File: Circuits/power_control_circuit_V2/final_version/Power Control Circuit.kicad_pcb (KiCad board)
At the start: 2 copper layers, 122.3 x 43.4 mm, 38 parts, among them Q10 IRF1405, Q12 IRF1405, Q2 S8050, Q3 S8550, Q4 IRF1405, Q6 S8050, Q7 S8550, Q8 IRF1405, Q9 IRF1405, U1 PC817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

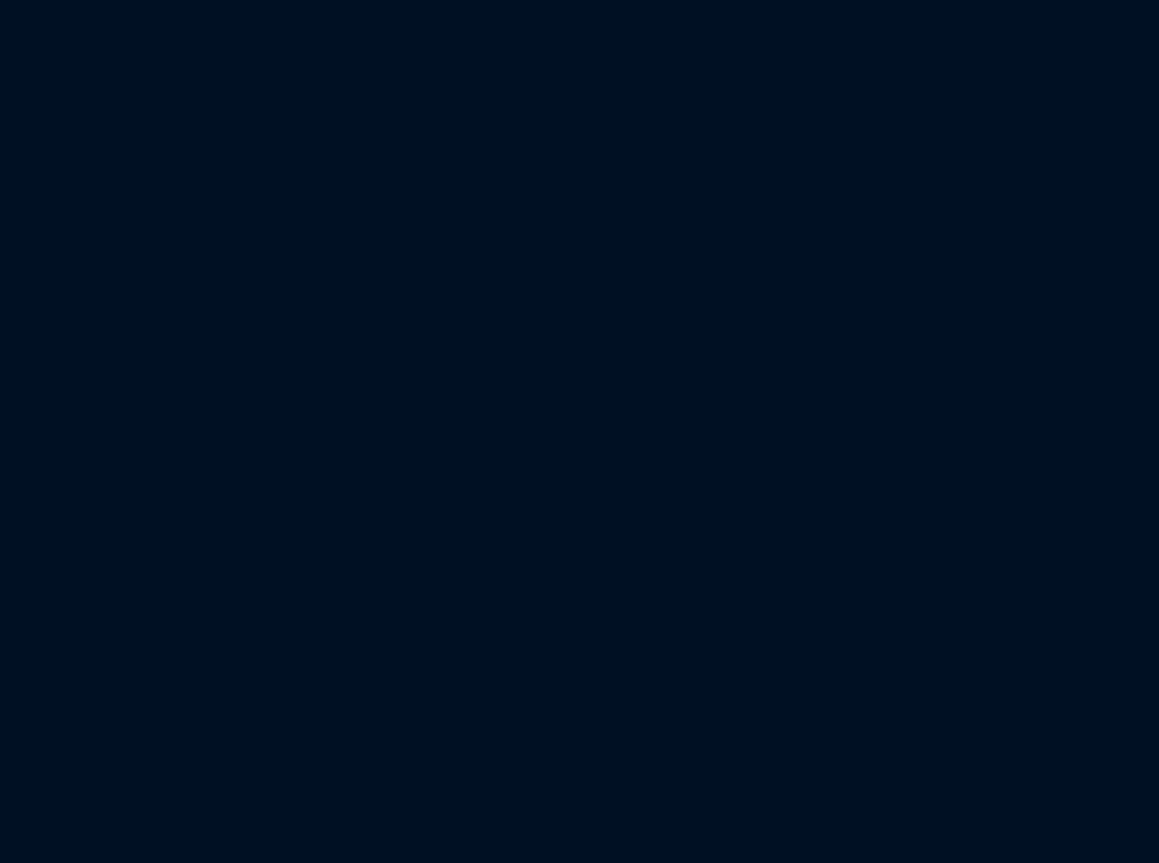
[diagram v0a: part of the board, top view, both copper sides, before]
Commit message: started pad changes
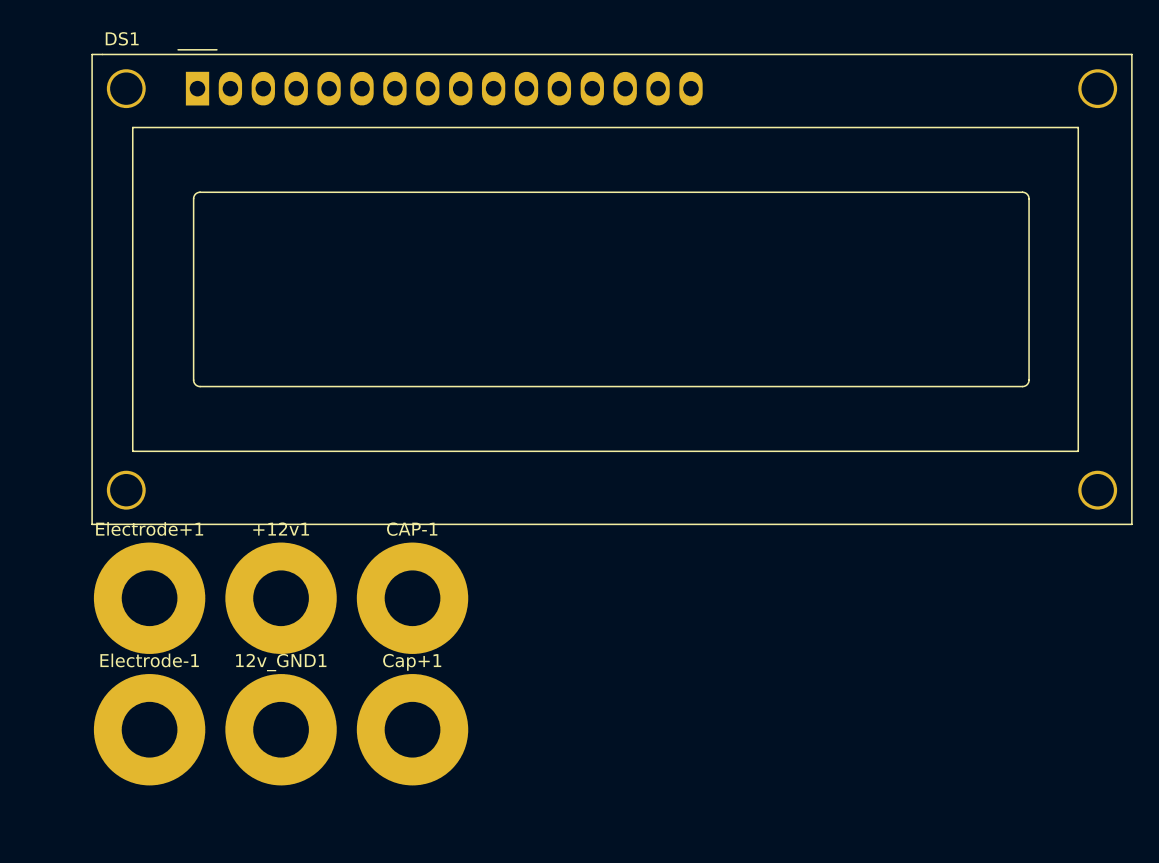
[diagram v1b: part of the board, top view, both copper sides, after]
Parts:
- added +12v1: Pin, MountingHole:MountingHole_4.3mm_M4_Pad, F.Cu at (108.0, 91.2)
- added 12v_GND1: Pin, MountingHole:MountingHole_4.3mm_M4_Pad, F.Cu at (108.0, 101.3)
- added CAP-1: Pin, MountingHole:MountingHole_4.3mm_M4_Pad, F.Cu at (118.2, 91.2)
- added Cap+1: Pin, MountingHole:MountingHole_4.3mm_M4_Pad, F.Cu at (118.2, 101.3)
- added DS1: WC1602A, Display:WC1602A, F.Cu at (101.6, 51.8)
- added Electrode+1: Pin, MountingHole:MountingHole_4.3mm_M4_Pad, F.Cu at (97.9, 91.2)
- added Electrode-1: Pin, MountingHole:MountingHole_4.3mm_M4_Pad, F.Cu at (97.9, 101.3)
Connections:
- net Net-(Q4-D) renamed /NMOS_CHARGE
- Q10 pad 1: Net-(Electrodes1-Pin_1) -> /NMOS_DISCHARGE
- Q12 pad 1: Net-(Electrodes1-Pin_1) -> /NMOS_DISCHARGE
- Q8 pad 1: Net-(Electrodes1-Pin_1) -> /NMOS_DISCHARGE
- Q9 pad 1: Net-(Electrodes1-Pin_1) -> /NMOS_DISCHARGE

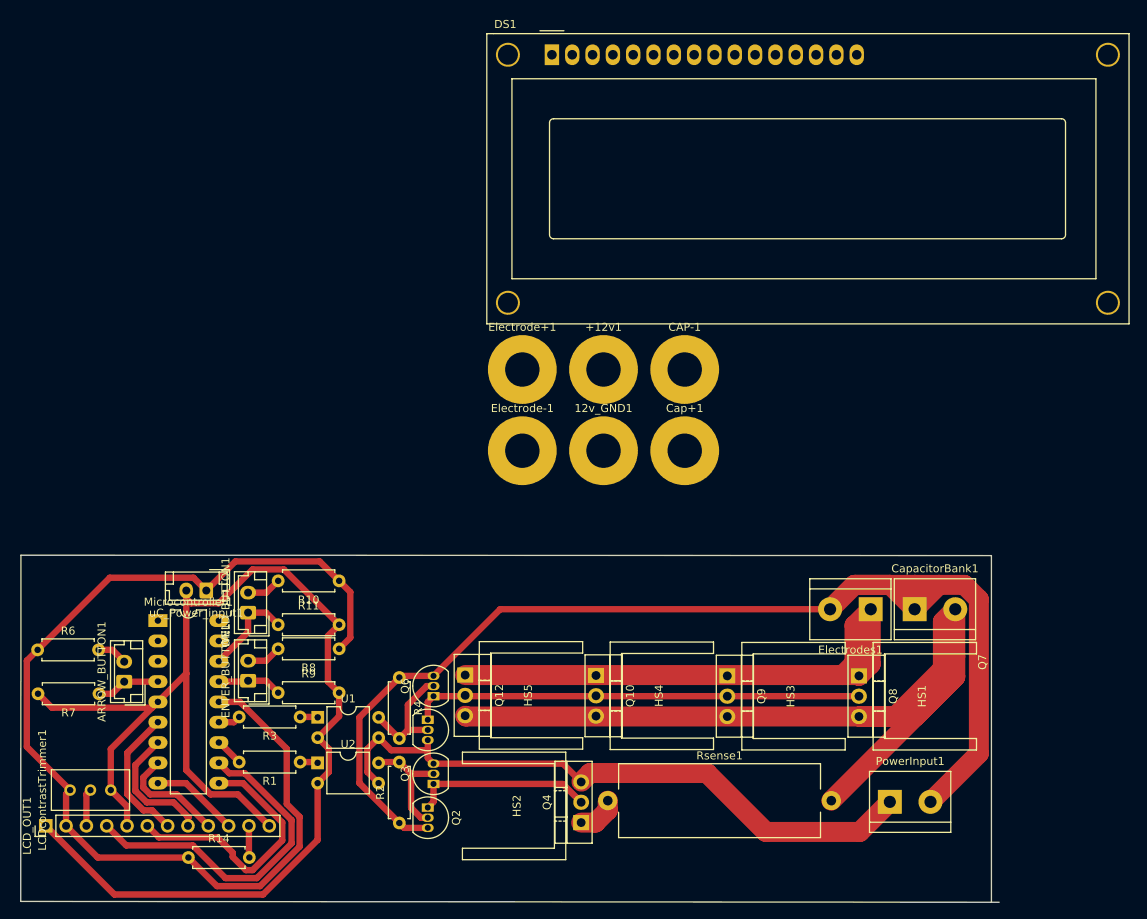
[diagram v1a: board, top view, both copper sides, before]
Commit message: added terminal pads to the pcb
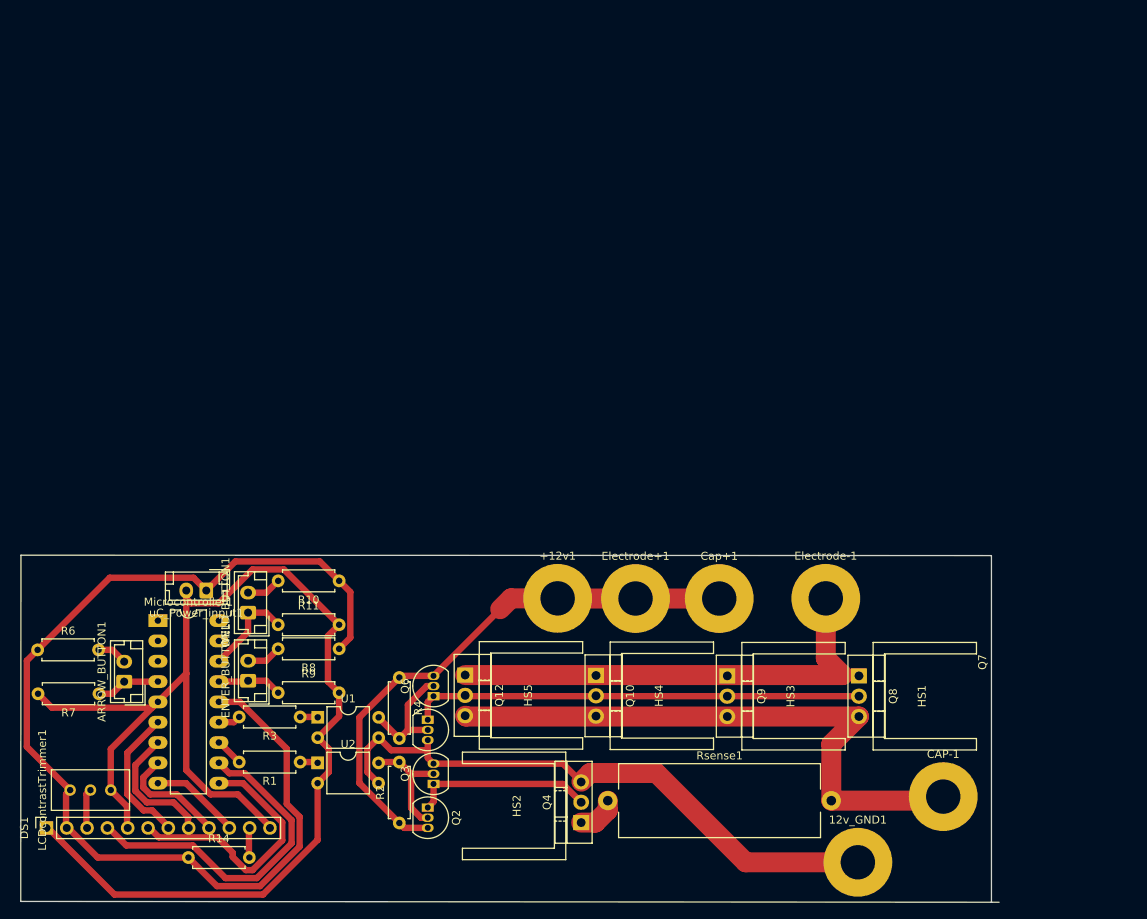
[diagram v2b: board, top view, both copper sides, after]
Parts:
- removed CapacitorBank1: CP, TerminalBlock:TerminalBlock_bornier-2_P5.08mm
- removed Electrodes1: Conn_01x02_Male, TerminalBlock:TerminalBlock_bornier-2_P5.08mm
- removed LCD_OUT1: Conn_01x12_Socket, Connector_PinHeader_2.54mm:PinHeader_1x12_P2.54mm_Vertical
- removed PowerInput1: Screw_Terminal_01x02, TerminalBlock:TerminalBlock_bornier-2_P5.08mm
- DS1: footprint Display:WC1602A -> Connector_PinSocket_2.54mm:PinSocket_1x12_P2.54mm_Vertical
- moved DS1 115.5 mm to (38.4, 148.5), turned to 90 degrees
- moved CAP-1 62.4 mm to (150.5, 144.6)
- moved 12v_GND1 60.5 mm to (139.8, 152.8)
- moved Electrode-1 42.2 mm to (135.8, 119.8)
- moved Electrode+1 31.9 mm to (112.0, 119.8)
- moved +12v1 29.2 mm to (102.3, 119.8)
- moved Cap+1 19.0 mm to (122.5, 119.8)
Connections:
- DS1 pad 10: unconnected-(DS1-D3-Pad10) -> D7
- DS1 pad 11: D4 -> LED+
- DS1 pad 12: D5 -> GND
- DS1 pad 7: unconnected-(DS1-D0-Pad7) -> D4
- DS1 pad 8: unconnected-(DS1-D1-Pad8) -> D5
- DS1 pad 9: unconnected-(DS1-D2-Pad9) -> D6
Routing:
- net +12V: track 148.1 -> 70.2 mm
- net Net-(Electrodes1-Pin_1): track 67.9 -> 0.00 mm
- net /NMOS_DISCHARGE: track 0.00 -> 57.7 mm
- net GNDS: track 117.0 -> 75.4 mm
- net GNDA: track 79.9 -> 75.9 mm

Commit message: redesigning the circuit
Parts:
- removed ARROW_BUTTON1, ENTER_BUTTON1, WELD_BUTTON1, uC_Power_input1: Conn_01x02_Socket, Connector_JST:JST_EH_B2B-EH-A_1x02_P2.50mm_Vertical
- removed HS1, HS2, HS3, HS4, HS5: Heatsink_Pad_2Pin, Heatsink:Heatsink_Stonecold_HS-S03_13.21x12.7mm
- removed LCDcontrastTrimmer1: 5kOhm, Potentiometer_THT:Potentiometer_Bourns_3386C_Horizontal
- removed Microcontroller1: PIC16F628A-IP, Package_DIP:DIP-18_W7.62mm_LongPads
- added ARROW1: JST-2P, Connector_JST:JST_EH_B2B-EH-A_1x02_P2.50mm_Vertical, F.Cu at (58.4, 104.1)
- added ENTER1: JST-2P, Connector_JST:JST_EH_B2B-EH-A_1x02_P2.50mm_Vertical, F.Cu at (80.0, 105.4)
- added Main-MCU1: PIC16F628A-IP, Package_DIP:DIP-18_W7.62mm_LongPads, F.Cu at (64.8, 96.5)
- added Power5v1: JST-2P, Connector_JST:JST_EH_B2B-EH-A_1x02_P2.50mm_Vertical, F.Cu at (55.4, 91.9)
- added Trimmer1: 5kOhm, Connector_PinSocket_2.54mm:PinSocket_1x03_P2.54mm_Vertical, F.Cu at (46.7, 124.2)
- added WELD1: JST-2P, Connector_JST:JST_EH_B2B-EH-A_1x02_P2.50mm_Vertical, F.Cu at (80.0, 96.5)
- moved Q12 73.2 mm to (160.5, 107.2), turned to 0 degrees
- moved Q10 46.9 mm to (148.3, 107.2), turned to 0 degrees
- moved Electrode+1 45.3 mm to (148.8, 93.5)
- moved +12v1 43.3 mm to (136.7, 93.5)
- moved R2 40.7 mm to (104.6, 113.8)
- moved Electrode-1 38.7 mm to (165.1, 94.5)
- moved Q2 36.1 mm to (111.3, 120.0), turned to 90 degrees
- moved Q6 34.2 mm to (111.3, 108.2)
- moved Q7 34.1 mm to (110.7, 111.5)
- moved Q4 32.6 mm to (128.0, 124.5), turned to 180 degrees
- moved Rsense1 32.1 mm to (134.4, 126.0)
- moved R11 31.8 mm to (85.6, 97.0)
- moved U1 31.6 mm to (93.5, 111.2)
- moved U2 30.9 mm to (93.5, 117.9)
- moved Q3 30.8 mm to (110.7, 123.7), turned to -90 degrees
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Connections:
- net LED+ renamed Net-(DS1-LED(+))
- DS1 pad 3: VO -> Net-(DS1-VO)
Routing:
- net GND: track 170.1 -> 0.00 mm
- net +5V: track 137.4 -> 0.00 mm
- net GNDA: track 75.9 -> 0.00 mm
- net GNDS: track 75.4 -> 0.00 mm
- net +12V: track 70.2 -> 0.00 mm
- net /NMOS_DISCHARGE: track 57.7 -> 0.00 mm
- net Net-(Q10-G): track 56.6 -> 0.00 mm
- net RS: track 42.6 -> 0.00 mm
- net EN: track 33.2 -> 0.00 mm
- net Net-(Q2-E): track 22.6 -> 0.00 mm
- net D4: track 17.3 -> 0.00 mm
- net D5: track 16.3 -> 0.00 mm
- net Net-(Q6-B): track 15.0 -> 0.00 mm
- net Net-(Q2-B): track 14.4 -> 0.00 mm
- net D6: track 14.0 -> 0.00 mm
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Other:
- board outline removed

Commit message: finished PCB (again)
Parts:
- added Bridge1: 0ohm, Resistor_THT:R_Axial_DIN0207_L6.3mm_D2.5mm_P5.08mm_Vertical, F.Cu at (69.1, 96.4)
- added C1: 220uF, Capacitor_THT:CP_Radial_D6.3mm_P2.50mm, F.Cu at (63.4, 92.9)
- added H1: MountingHole, MountingHole:MountingHole_3.2mm_M3_DIN965_Pad_TopBottom, F.Cu at (79.0, 123.0)
- added H2: MountingHole, MountingHole:MountingHole_3.2mm_M3_DIN965_Pad_TopBottom, F.Cu at (100.0, 93.0)
- added H3: MountingHole, MountingHole:MountingHole_3.2mm_M3_DIN965_Pad_TopBottom, F.Cu at (152.0, 93.0)
- Q2, Q3, Q6, Q7: footprint Package_TO_SOT_THT:TO-92_Inline -> Package_TO_SOT_THT:TO-92_Inline_Wide
- R-Shunt1: renamed from Rsense1; value 1 -> 2ohm
- R14: footprint Resistor_THT:R_Axial_DIN0207_L6.3mm_D2.5mm_P7.62mm_Horizontal -> Resistor_THT:R_Axial_DIN0309_L9.0mm_D3.2mm_P12.70mm_Horizontal
- moved DS1 34.5 mm to (45.7, 94.1), turned to 0 degrees
- moved 12v_GND1 32.3 mm to (112.6, 120.0)
- moved R14 28.2 mm to (50.5, 106.7), turned to -90 degrees
- moved Trimmer1 27.8 mm to (50.1, 96.6), turned to 0 degrees
- moved CAP-1 25.2 mm to (151.8, 108.2)
- moved Electrode-1 21.9 mm to (143.4, 96.9)
- moved Power5v1 18.8 mm to (74.2, 92.7)
- moved Q12 18.5 mm to (142.2, 104.9), turned to -90 degrees
- moved Q10 17.5 mm to (131.0, 104.9), turned to -90 degrees
- moved Electrode+1 17.5 mm to (131.6, 96.9)
- moved Q9 15.9 mm to (119.9, 104.9), turned to -90 degrees
- moved +12v1 15.4 mm to (121.6, 96.9)
- moved Q8 15.0 mm to (108.7, 104.9), turned to -90 degrees
- moved R4 14.7 mm to (98.7, 104.2)
- moved R7 14.6 mm to (59.8, 102.2), turned to -90 degrees
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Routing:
- net GND: track 0.00 -> 175.8 mm
- net GNDS: track 0.00 -> 136.1 mm
- net +5V: track 0.00 -> 129.5 mm
- net +12V: track 0.00 -> 120.6 mm
- net /NMOS_DISCHARGE: track 0.00 -> 97.2 mm
- net RS: track 0.00 -> 65.8 mm
- net GNDA: track 0.00 -> 60.0 mm
- net EN: track 0.00 -> 48.9 mm
- net Net-(Q10-G): track 0.00 -> 42.0 mm
- net Net-(Q2-E): track 0.00 -> 25.3 mm
- net Net-(Q6-B): track 0.00 -> 20.9 mm
- net D4: track 0.00 -> 20.5 mm
- net D6: track 0.00 -> 20.0 mm
- net weldingkey: track 0.00 -> 19.9 mm
- net D7: track 0.00 -> 19.7 mm
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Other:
- board outline added: 116.9 x 37.5 mm

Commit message: minor changes
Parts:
- moved H2 1.00 mm to (99.0, 93.0)
- moved H3 0.96 mm to (153.0, 93.0)
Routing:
- net GND: track 175.8 -> 182.1 mm
- net Net-(R3-Pad1): track 12.7 -> 6.51 mm
- net +5V: track 129.5 -> 132.4 mm

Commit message: minor changes
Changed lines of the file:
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@@
   (segment (start 55.4936 96.2714) (end 55.4936 92.6392) (width 1) (layer "F.Cu") (net 2))
   (segment (start 55.4936 96.2714) (end 56.7468 97.5246) (width 1) (layer "F.Cu") (net 2))
+  (segment (start 92.0242 112.522) (end 92.0242 121.6152) (width 1) (layer "F.Cu") (net 3))
   (segment (start 102.362 124.587) (end 103.1748 124.587) (width 1) (layer "F.Cu") (net 3))
   (segment (start 114.0968 94.361) (end 119.126 94.361) (width 2.5) (layer "F.Cu") (net 3))
@@
   (segment (start 121.6406 96.8756) (end 124.1044 94.4118) (width 2.5) (layer "F.Cu") (net 3))
   (segment (start 131.6482 96.8502) (end 111.6076 96.8502) (width 2.5) (layer "F.Cu") (net 3))
+  (segment (start 92.0242 121.6152) (end 94.8182 124.4092) (width 1) (layer "F.Cu") (net 3))
   (segment (start 102.362 124.587) (end 102.1842 124.4092) (width 1) (layer "F.Cu") (net 3))
   (segment (start 111.6076 96.8502) (end 113.9952 99.2378) (width 2.5) (layer "F.Cu") (net 3))
@@
   (segment (start 124.079 99.314) (end 129.1844 99.314) (width 2.5) (layer "F.Cu") (net 3))
   (segment (start 96.139 104.1654) (end 98.679 104.1654) (width 1) (layer "F.Cu") (net 3))
-  (segment (start 96.139 105.7656) (end 93.6752 108.2294) (width 1) (layer "F.Cu") (net 3))
+  (segment (start 93.6752 108.2294) (end 93.6752 110.871) (width 1) (layer "F.Cu") (net 3))
   (segment (start 121.6406 96.8756) (end 124.079 99.314) (width 2.5) (layer "F.Cu") (net 3))
   (segment (start 113.9952 99.2378) (end 119.2784 99.2378) (width 2.5) (layer "F.Cu") (net 3))
-  (segment (start 93.6752 109.9058) (end 92.3022 111.2788) (width 1) (layer "F.Cu") (net 3))
+  (segment (start 93.6752 110.871) (end 92.0242 112.522) (width 1) (layer "F.Cu") (net 3))
   (segment (start 124.1044 94.4118) (end 129.2098 94.4118) (width 2.5) (layer "F.Cu") (net 3))
-  (segment (start 92.2542 121.8452) (end 94.8182 124.4092) (width 1) (layer "F.Cu") (net 3))
-  (segment (start 92.3022 121.7972) (end 92.2542 121.8452) (width 1) (layer "F.Cu") (net 3))
+  (segment (start 96.139 105.7656) (end 93.6752 108.2294) (width 1) (layer "F.Cu") (net 3))
   (segment (start 96.139 104.1654) (end 102.5398 97.7646) (width 1) (layer "F.Cu") (net 3))
   (segment (start 102.5398 97.7646) (end 103.9114 97.7646) (width 1) (layer "F.Cu") (net 3))
+  (segment (start 119.2784 99.2378) (end 121.6406 96.8756) (width 2.5) (layer "F.Cu") (net 3))
+  (segment (start 129.2098 94.4118) (end 131.6482 96.8502) (width 2.5) (layer "F.Cu") (net 3))
   (segment (start 94.8182 124.4092) (end 98.6282 124.4092) (width 1) (layer "F.Cu") (net 3))
-  (segment (start 92.3022 111.2788) (end 92.3022 121.7972) (width 1) (layer "F.Cu") (net 3))
-  (segment (start 119.2784 99.2378) (end 121.6406 96.8756) (width 2.5) (layer "F.Cu") (net 3))
   (segment (start 96.139 104.1654) (end 96.139 105.7656) (width 1) (layer "F.Cu") (net 3))
-  (segment (start 129.2098 94.4118) (end 131.6482 96.8502) (width 2.5) (layer "F.Cu") (net 3))
   (segment (start 119.126 94.361) (end 121.6406 96.8756) (width 2.5) (layer "F.Cu") (net 3))
-  (segment (start 93.6752 108.2294) (end 93.6752 109.9058) (width 1) (layer "F.Cu") (net 3))
   (segment (start 108.7374 111.3028) (end 109.1692 111.7346) (width 1.8) (layer "F.Cu") (net 4))
   (segment (start 151.8412 112.5982) (end 151.8412 114.8588) (width 2.5) (layer "F.Cu") (net 4))
